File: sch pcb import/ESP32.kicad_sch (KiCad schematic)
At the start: 43 parts, among them J301 USB_C_Receptacle_USB2.0_16P, J302 Conn_01x04_Pin, Q301 SS8050, Q302 SS8050, U301 FT232RL, U302 ESP32-S3-WROOM-1, U303 USB6B1RL

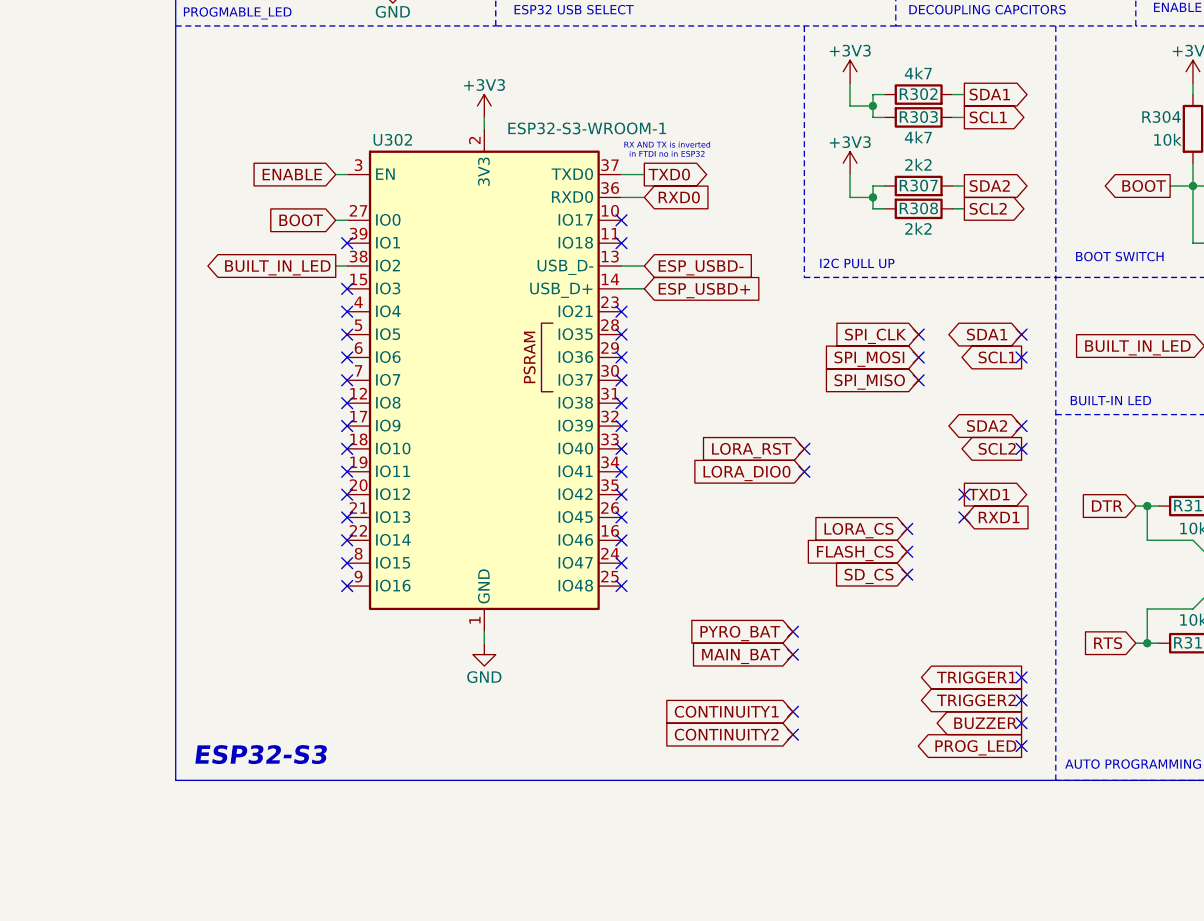
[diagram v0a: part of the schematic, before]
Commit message: added servo and finished esp32 connections
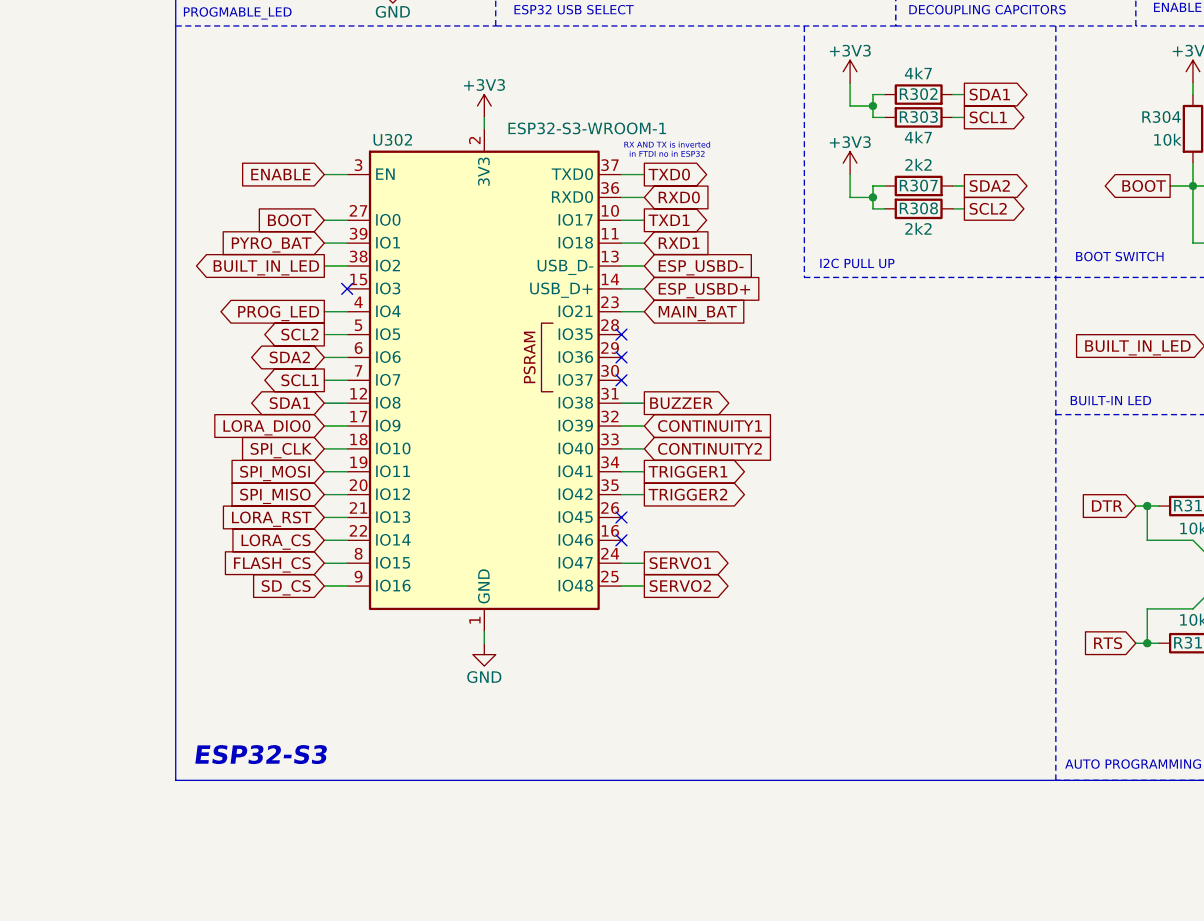
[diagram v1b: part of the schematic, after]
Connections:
- net BUZZER: now also U302.31 (IO38)
- net CONTINUITY1: now also U302.32 (IO39)
- net CONTINUITY2: now also U302.33 (IO40)
- net FLASH_CS: now also U302.8 (IO15)
- net LORA_CS: now also U302.22 (IO14)
- net LORA_DIO0: now also U302.17 (IO9)
- net LORA_RST: now also U302.21 (IO13)
- net MAIN_BAT: now also U302.23 (IO21)
- net PROG_LED: now also U302.4 (IO4)
- net PYRO_BAT: now also U302.39 (IO1)
- net RXD1: now also U302.11 (IO18)
- net SCL1: now also U302.7 (IO7)
- net SCL2: now also U302.5 (IO5)
- net SDA1: now also U302.12 (IO8)
- net SDA2: now also U302.6 (IO6)
- net SD_CS: now also U302.9 (IO16)
- net SPI_CLK: now also U302.18 (IO10)
- net SPI_MISO: now also U302.20 (IO12)
- net SPI_MOSI: now also U302.19 (IO11)
- net TRIGGER1: now also U302.34 (IO41)
- net TRIGGER2: now also U302.35 (IO42)
- net TXD1: now also U302.10 (IO17)
- net SERVO1: now reaches U302.24 (IO47)
- net SERVO2: now reaches U302.25 (IO48)
- no-connect marks 65 -> 19
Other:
- company: Done by :- Arudhran -> Drawn by :- Arudhran
- title: AVIONICS PCB -> VECTRON

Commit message: rearranging for aesthetics
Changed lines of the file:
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@@
 	(text "RX TX\nLEDS\n"
 		(exclude_from_sim no)
-		(at 92.71 62.484 0)
+		(at 92.456 62.484 0)
 		(effects
 			(font
@@
 	(text "BOOT SWITCH\n"
 		(exclude_from_sim no)
-		(at 247.142 67.818 0)
+		(at 245.872 68.58 0)
 		(effects
 			(font

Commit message: minor changes
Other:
- title: VECTRON -> VECTRON-V1
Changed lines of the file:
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@@
 	(paper "A4")
 	(title_block
-		(title "VECTRON")
-		(date "2025-06-10")
+		(title "VECTRON-V1")
+		(date "2025-06-13")
 		(rev "1.0.0")
 		(company "Drawn by :- Arudhran")

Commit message: minor changes
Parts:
- C301, C302, C303, C304, C305, C306, C307, C308, C309, C310, C311, C312, C313: footprint (none) -> Capacitor_SMD:C_0603_1608Metric
- D302, D303, D304: footprint (none) -> LED_SMD:LED_0603_1608Metric
- J301: footprint (none) -> Connector_USB:USB_C_Receptacle_GCT_USB4105-xx-A_16P_TopMnt_Horizontal
- JP301, JP302, JP303: footprint (none) -> Jumper:SolderJumper-2_P1.3mm_Open_RoundedPad1.0x1.5mm
- R301, R302, R303, R304, R305, R306, R307, R308, R309, R310, R311, R312, R313, R314: footprint (none) -> Resistor_SMD:R_0603_1608Metric
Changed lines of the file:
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@@
 			)
 		)
-		(property "Footprint" ""
+		(property "Footprint" "Capacitor_SMD:C_0603_1608Metric"
 			(at 86.0552 137.16 0)
 			(effects
@@
 			)
 		)
-		(property "Footprint" ""
+		(property "Footprint" "Resistor_SMD:R_0603_1608Metric"
 			(at 253.492 53.34 90)
 			(effects
@@
 			)
 		)
-		(property "Footprint" ""
+		(property "Footprint" "Resistor_SMD:R_0603_1608Metric"
 			(at 255.27 112.268 90)
 			(effects
@@
 			)
 		)
-		(property "Footprint" ""
+		(property "Footprint" "Resistor_SMD:R_0603_1608Metric"
 			(at 255.27 97.028 90)
 			(effects
@@
 			)
 		)
-		(property "Footprint" ""
+		(property "Footprint" "Connector_USB:USB_C_Receptacle_GCT_USB4105-xx-A_16P_TopMnt_Horizontal"
 			(at 34.29 144.78 0)
 			(effects
@@
 			)
 		)
-		(property "Footprint" ""
+		(property "Footprint" "Resistor_SMD:R_0603_1608Metric"
 			(at 53.34 138.938 90)
 			(effects
@@
 			)
 		)
-		(property "Footprint" ""
+		(property "Footprint" "Resistor_SMD:R_0603_1608Metric"
 			(at 224.79 61.468 90)
 			(effects
@@
 			)
 		)
-		(property "Footprint" ""
+		(property "Footprint" "Resistor_SMD:R_0603_1608Metric"
 			(at 224.79 60.452 90)
 			(effects
@@
 			)
 		)
-		(property "Footprint" ""
+		(property "Footprint" "Capacitor_SMD:C_0603_1608Metric"
 			(at 229.5652 30.48 0)
 			(effects
@@
 			)
 		)
-		(property "Footprint" ""
+		(property "Footprint" "Resistor_SMD:R_0603_1608Metric"
 			(at 261.62 75.692 90)
 			(effects
@@
 			)
 		)
-		(property "Footprint" ""
+		(property "Footprint" "Capacitor_SMD:C_0603_1608Metric"
 			(at 244.8052 30.48 0)
 			(effects
@@
 			)
 		)
-		(property "Footprint" ""
+		(property "Footprint" "Jumper:SolderJumper-2_P1.3mm_Open_RoundedPad1.0x1.5mm"
 			(at 199.39 25.4 0)
 			(effects
@@
 			)
 		)
-		(property "Footprint" ""
+		(property "Footprint" "Resistor_SMD:R_0603_1608Metric"
 			(at 53.34 136.398 90)
 			(effects
@@
 			)
 		)
-		(property "Footprint" ""
+		(property "Footprint" "Capacitor_SMD:C_0603_1608Metric"
 			(at 237.1852 30.48 0)
 			(effects
@@
 			)
 		)
-		(property "Footprint" ""
+		(property "Footprint" "Jumper:SolderJumper-2_P1.3mm_Open_RoundedPad1.0x1.5mm"
 			(at 38.1 182.88 0)
 			(effects
@@
 			)
 		)
-		(property "Footprint" ""
+		(property "Footprint" "Capacitor_SMD:C_0603_1608Metric"
 			(at 102.5652 137.16 0)
 			(effects
@@
 			)
 		)
-		(property "Footprint" ""
+		(property "Footprint" "Resistor_SMD:R_0603_1608Metric"
 			(at 81.28 57.912 90)
 			(effects
@@
 			)
 		)
-		(property "Footprint" ""
+		(property "Footprint" "LED_SMD:LED_0603_1608Metric"
 			(at 95.25 49.53 0)
 			(effects
@@
 			)
 		)
-		(property "Footprint" ""
+		(property "Footprint" "Resistor_SMD:R_0603_1608Metric"
 			(at 259.842 25.4 90)
 			(effects
@@
 			)
 		)
-		(property "Footprint" ""
+		(property "Footprint" "Capacitor_SMD:C_0603_1608Metric"
 			(at 41.91 171.7548 0)
 			(effects
@@
 			)
 		)
-		(property "Footprint" ""
+		(property "Footprint" "LED_SMD:LED_0603_1608Metric"
 			(at 275.59 77.47 0)
 			(effects
@@
 			)
 		)
-		(property "Footprint" ""
+		(property "Footprint" "Jumper:SolderJumper-2_P1.3mm_Open_RoundedPad1.0x1.5mm"
 			(at 199.39 27.94 0)
 			(effects
@@
 			)
 		)
-		(property "Footprint" ""
+		(property "Footprint" "Capacitor_SMD:C_0603_1608Metric"
 			(at 273.05 37.1348 0)
 			(effects
@@
 			)
 		)
-		(property "Footprint" ""
+		(property "Footprint" "Capacitor_SMD:C_0603_1608Metric"
 			(at 94.9452 137.16 0)
 			(effects
@@
 			)
 		)
-		(property "Footprint" ""
+		(property "Footprint" "Capacitor_SMD:C_0603_1608Metric"
 			(at 27.6352 64.77 0)
 			(effects
@@
 			)
 		)
-		(property "Footprint" ""
+		(property "Footprint" "LED_SMD:LED_0603_1608Metric"
 			(at 90.17 49.53 0)
 			(effects
@@
 			)
 		)
-		(property "Footprint" ""
+		(property "Footprint" "Capacitor_SMD:C_0603_1608Metric"
 			(at 28.9052 29.21 0)
 			(effects
@@
 			)
 		)
-		(property "Footprint" ""
+		(property "Footprint" "Resistor_SMD:R_0603_1608Metric"
 			(at 224.79 51.308 90)
 			(effects
@@
 			)
 		)
-		(property "Footprint" ""
+		(property "Footprint" "Capacitor_SMD:C_0603_1608Metric"
 			(at 20.0152 64.77 0)
 			(effects
@@
 			)
 		)
-		(property "Footprint" ""
+		(property "Footprint" "Resistor_SMD:R_0603_1608Metric"
 			(at 224.79 50.292 90)
 			(effects
@@
 			)
 		)
-		(property "Footprint" ""
+		(property "Footprint" "Resistor_SMD:R_0603_1608Metric"
 			(at 38.1 179.578 90)
 			(effects
@@
 			)
 		)
-		(property "Footprint" ""
+		(property "Footprint" "Resistor_SMD:R_0603_1608Metric"
 			(at 81.28 58.928 90)
 			(effects
@@
 			)
 		)
-		(property "Footprint" ""
+		(property "Footprint" "Capacitor_SMD:C_0603_1608Metric"
 			(at 266.7 65.0748 0)
 			(effects
@@
 			)
 		)
-		(property "Footprint" ""
+		(property "Footprint" "Capacitor_SMD:C_0603_1608Metric"
 			(at 78.4352 137.16 0)
 			(effects

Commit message: minor changes
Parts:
- C301: value 10uf -> 100nf
- S301, S302: footprint digikey-footprints:Switch_Tactile_SMD_4.5x4.5mm_TL3315NF160Q -> Tact switch:tact switch 3.4x2.5mm
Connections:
- net USBD+: now also J302.1 (Pin_1); no longer J302.2 (Pin_2)
- net USBD-: now also J302.2 (Pin_2); no longer J302.1 (Pin_1)
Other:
- company: Drawn by :- Arudhran -> (none)
